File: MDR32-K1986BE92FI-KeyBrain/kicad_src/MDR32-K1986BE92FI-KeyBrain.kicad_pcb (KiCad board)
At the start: 2 copper layers, 18.1 x 33.3 mm, 30 parts, among them J2 Conn_01x12, J3 USB_C_Receptacle_USB2.0_16P, U1 AP2112K-3.3, U2 K1986BE92FI, U3 USBLC6-2SC6, U4 ProMicro, Y1 8MHz

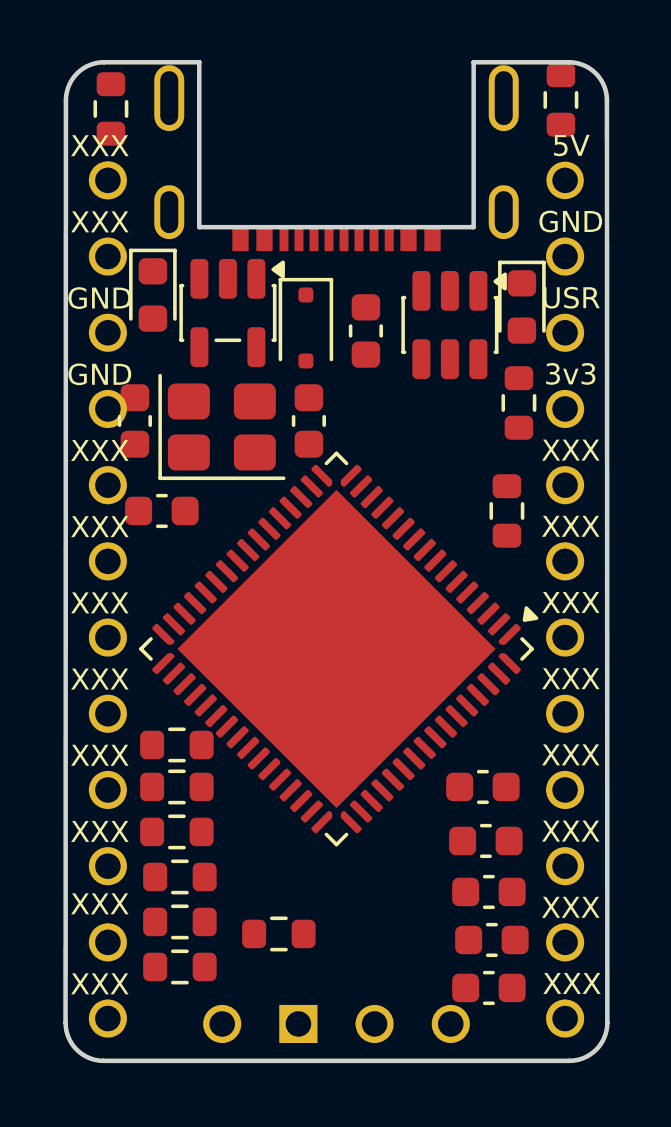
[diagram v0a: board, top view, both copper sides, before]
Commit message: fix usb footprint
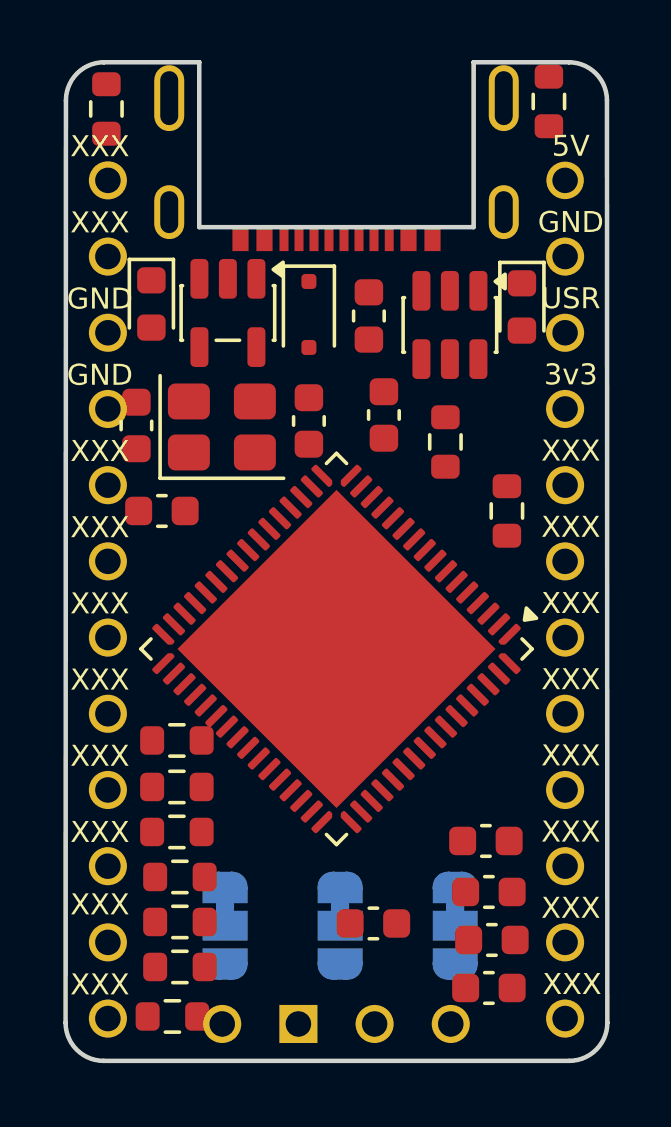
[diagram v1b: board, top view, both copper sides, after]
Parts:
- removed D4: 3A/10V/280mV, Diode_SMD:D_SOD-323F
- removed F3: 6V 0.5A MF-FSMF050X-2, Fuse:Fuse_0603_1608Metric
- added C8: 0.1μF, Capacitor_SMD:C_0603_1608Metric, F.Cu at (82.0, 89.3)
- added D2: RED, LED_SMD:LED_0603_1608Metric, F.Cu at (74.7, 68.7)
- added F1: 6V 0.5A MF-FSMF050X-2, Fuse:Fuse_0603_1608Metric, F.Cu at (81.9, 69.1)
- added JP1: MODE0, Jumper:SolderJumper-3_P1.3mm_Bridged12_RoundedPad1.0x1.5mm, B.Cu at (77.1, 89.4)
- added JP2: MODE1, Jumper:SolderJumper-3_P1.3mm_Bridged12_RoundedPad1.0x1.5mm, B.Cu at (80.9, 89.4)
- added JP3: MODE2, Jumper:SolderJumper-3_P1.3mm_Bridged12_RoundedPad1.0x1.5mm, B.Cu at (84.8, 89.4)
- C1: value 0.1μF -> 1μF
- C2: value 1μF -> 10pF
- C5: value 0.1μF -> 10pF
- C7: value 10pF -> 0.1μF
- D1: value RED -> 3A/10V/280mV; footprint LED_SMD:LED_0603_1608Metric -> Diode_SMD:D_SOD-323F
- J1: renamed from J3; value USB_C_Receptacle_USB2.0_16P -> USB-C USB 2.0 MC-372
- J2: value Conn_01x12 -> Conn_01x04
- R1, R2: value 5.1K -> 10K
- R8, R9: value 10K -> 5.1K
- moved R2 33.2 mm to (75.3, 92.5), turned to 0 degrees
- moved R8 29.2 mm to (87.9, 62.0), turned to -90 degrees
- moved R9 21.3 mm to (73.2, 62.2), turned to -90 degrees
- moved R1 21.2 mm to (75.5, 83.2), turned to 180 degrees
- moved C2 16.7 mm to (74.2, 72.8), turned to 90 degrees
- moved C7 8.30 mm to (82.4, 72.4)
- moved D1 5.24 mm to (79.9, 69.0)
- moved R10 2.77 mm to (84.5, 73.3)
- renumbered D2 to D3, U3 to U2, U2 to U3
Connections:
- C2 pad 1: VBUS -> /OSC_IN
- C4 pad 1: +3.3V -> VBUS
- C5 pad 1: +3.3V -> /OSC_OUT
- C7 pad 1: /OSC_IN -> +3.3V
- D1 pad 1: GND -> +5V
- D3 pad 2: Net-(D2-A) -> Net-(D3-A)
- J1 pad A5: Net-(J3-CC1) -> Net-(J1-CC1)
- J1 pad B5: Net-(J3-CC2) -> Net-(J1-CC2)
- J1 pad S1: (no net) -> unconnected-(J1-SHIELD-PadS1)_3
- J2 pad 1: +5V -> +3.3V
- J2 pad 2: GND -> /DIO
- J2 pad 3: /USRBTN -> /CLK
- J2 pad 4: +3.3V -> GND
- R1 pad 1: Net-(J3-CC2) -> /DIO
- R1 pad 2: GND -> +3.3V
- R10 pad 2: /USRLED -> +3.3V
- R11 pad 1: Net-(D1-A) -> Net-(D3-A)
- R11 pad 2: +3.3V -> /USRLED
- R2 pad 1: Net-(J3-CC1) -> /CLK
- R2 pad 2: GND -> +3.3V
- R3 pad 1: /SWDIO -> /JAnTRS
- R4 pad 1: /SWDIO -> /JATDI
- R5 pad 1: /JAnTRS -> /JATDO
- R6 pad 1: /JATDI -> /nRESET
- R7 pad 1: /JATDO -> /WAKEUP
- R8 pad 1: /nRESET -> Net-(J1-CC2)
- R8 pad 2: +3.3V -> GND
- R9 pad 1: /WAKEUP -> Net-(J1-CC1)
- R9 pad 2: +3.3V -> GND
- U3 pad 29: unconnected-(U2-PD7-Pad29) -> /4
- U3 pad 36: unconnected-(U2-PD6-Pad36) -> /6
- U3 pad 41: /3/SCL -> /2/SDA
- U3 pad 42: /2/SDA -> /3/SCL
- U3 pad 44: /SWDIO -> /DIO
- U3 pad 45: /SWCLK -> /CLK
- U3 pad 58: unconnected-(U2-PA5-Pad58) -> /5
- U3 pad 59: unconnected-(U2-PA4-Pad59) -> /USRLED
- U3 pad 6: /JTAG_MODE -> /JTAG_MODE1
- U3 pad 63: unconnected-(U2-PA0-Pad63) -> /7
- U3 pad 7: GND -> /JTAG_MODE2
- U3 pad 8: GND -> /JTAG_MODE3

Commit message: MDR32-K1986BE92FI-KeyBrain: загружаем net-лист и обновляем измененные элементы
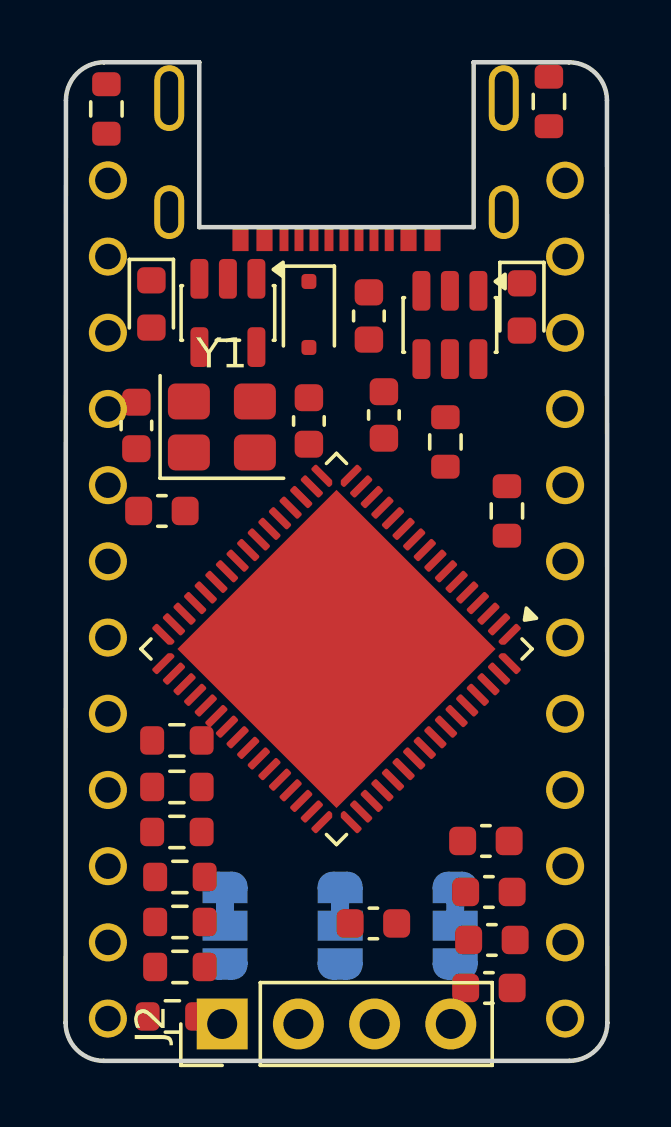
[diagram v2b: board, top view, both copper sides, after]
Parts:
- J1: footprint nrfmicro:USB-C_C168688 -> MDR32-K1986BE92FI-KeyBrain:USB-C_C168688
- J2: value Conn_01x04 -> SWD; footprint nrfmicro:connector_swd -> Connector_PinHeader_2.54mm:PinHeader_1x04_P2.54mm_Vertical
- U4: footprint nrfmicro:pro_micro -> MDR32-K1986BE92FI-KeyBrain:pro_micro
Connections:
- J1 pad S1: unconnected-(J1-SHIELD-PadS1)_3 -> (no net)

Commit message: MDR32-K1986BE92FI-KeyBrain: микроправки
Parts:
- J2: moved to B.Cu
- turned J2 to -90 degrees
